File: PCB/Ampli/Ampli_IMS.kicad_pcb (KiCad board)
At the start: 2 copper layers, 67 x 32 mm, 22 parts, among them J1 5227161-3, J2 5227161-3, J3 Conn_01x03_Male, SW1 SS22D0205G2, U1 LT1464CS8, U2 LMP7721

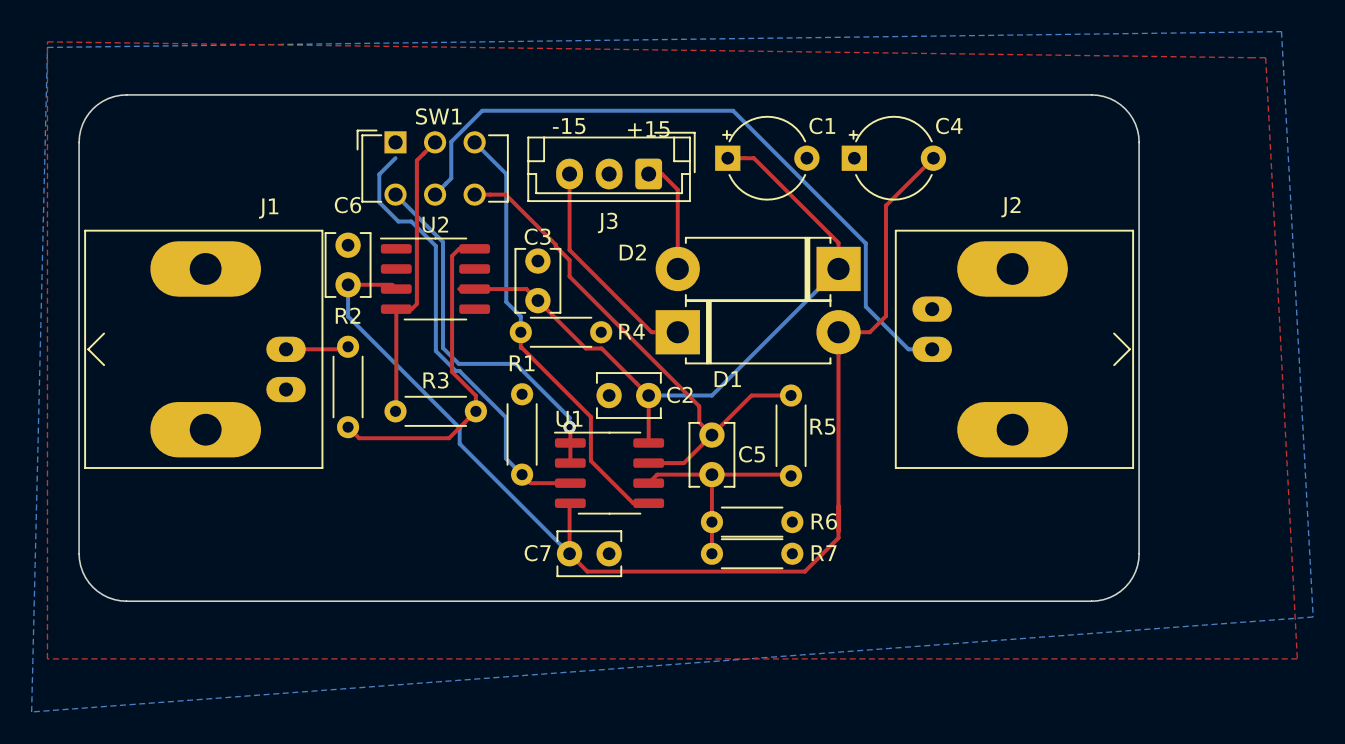
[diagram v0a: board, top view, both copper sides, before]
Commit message: Delete tracks
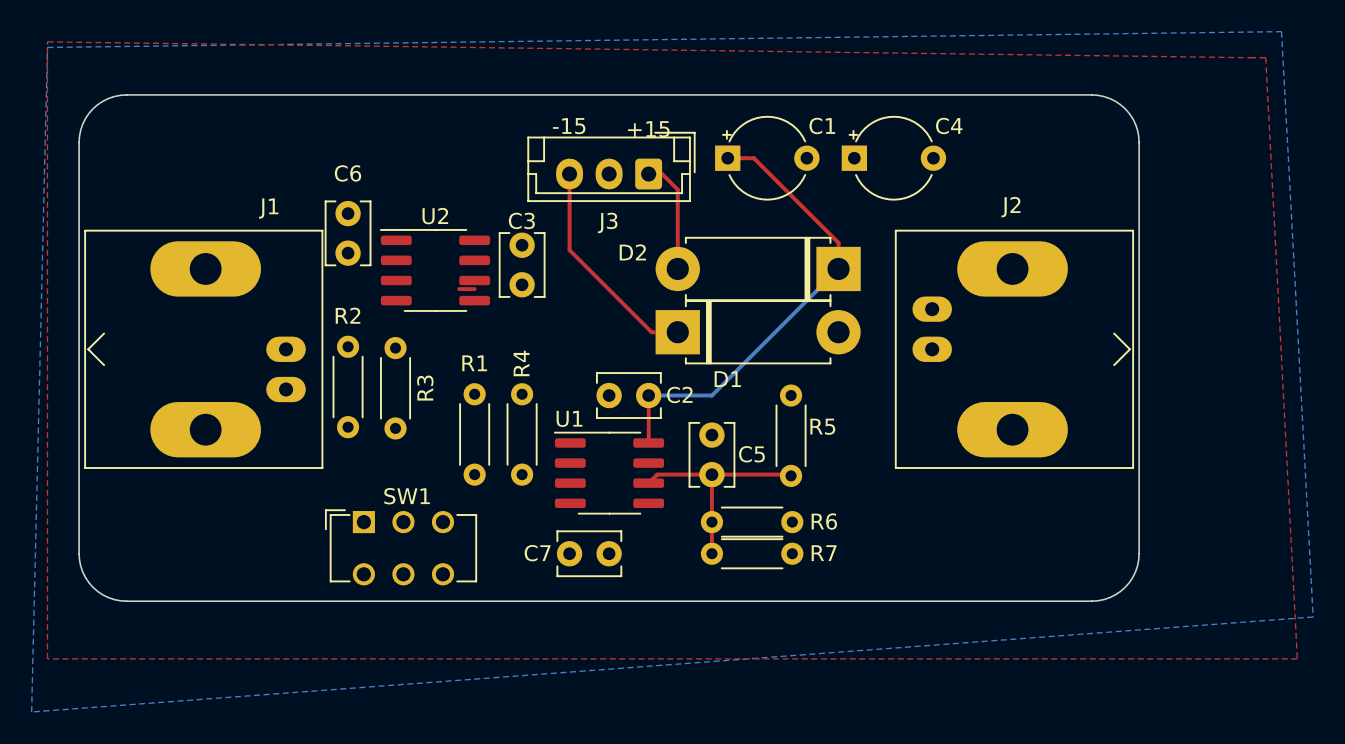
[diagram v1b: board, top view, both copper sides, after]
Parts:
- moved SW1 24.1 mm to (36.0, 45.0)
- moved R4 9.00 mm to (46.0, 42.0), turned to 90 degrees
- moved R3 4.00 mm to (38.0, 34.0), turned to 270 degrees
- moved R1 3.00 mm to (43.0, 42.0)
- moved C6 2.00 mm to (35.0, 28.0)
- moved C3 1.41 mm to (46.0, 30.0)
- moved U2 0.54 mm to (40.5, 29.1)
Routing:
- net /-15V: track 76.8 -> 0.00 mm
- net Net-(J2-Pad1): track 43.6 -> 0.00 mm
- net Net-(C5-Pad1): track 33.3 -> 0.00 mm
- net Net-(R1-Pad1): track 28.1 -> 0.00 mm
- net Net-(R4-Pad1): track 28.0 -> 0.00 mm
- net Net-(SW1-Pad4): track 23.7 -> 0.00 mm, vias 1 -> 0
- net Net-(R2-Pad1): track 21.1 -> 0.00 mm
- net Net-(R3-Pad1): track 18.7 -> 0.00 mm
- net /+15V: track 43.9 -> 30.2 mm
- net Net-(J1-Pad1): track 3.99 -> 0.00 mm

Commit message: Moved parts
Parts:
- moved C3 15.7 mm to (32.0, 23.0)
- moved R2 10.0 mm to (35.0, 29.0), turned to 270 degrees
- moved C6 9.85 mm to (44.0, 24.0)
- moved R3 6.40 mm to (42.0, 29.0), turned to 180 degrees
- moved U2 4.81 mm to (38.0, 25.0), turned to 180 degrees
- moved R1 2.83 mm to (41.0, 40.0)
- moved R4 2.83 mm to (44.0, 40.0)
- moved SW1 1.30 mm to (36.0, 43.7)
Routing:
- net /+15V: track 30.2 -> 10.9 mm
- net Net-(C5-Pad2): track 14.3 -> 10.0 mm

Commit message: tracks realised
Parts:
- removed the U2 at (38.0, 25.0)
- added U1: ADA4625-1, Package_SO:SO-8_3.9x4.9mm_P1.27mm, F.Cu at (37.4, 22.0)
- U2: renamed from U1; footprint Package_SO:SOIC-8_3.9x4.9mm_P1.27mm -> Package_SO:SO-8_3.9x4.9mm_P1.27mm
- moved R5 7.07 mm to (58.0, 42.0)
- moved R7 6.08 mm to (52.0, 48.0), turned to 180 degrees
- moved R6 6.00 mm to (52.0, 45.0), turned to 180 degrees
- moved C5 5.41 mm to (55.0, 44.0)
- moved C7 5.10 mm to (50.0, 42.0), turned to 180 degrees
- moved R4 5.00 mm to (44.0, 45.0)
- moved R3 4.47 mm to (38.0, 27.0), turned to 270 degrees
- moved U2 4.46 mm to (51.0, 37.5)
- moved C6 4.12 mm to (43.0, 20.0), turned to 270 degrees
- moved C2 3.16 mm to (57.0, 36.0), turned to 270 degrees
- moved D1 2.00 mm to (66.0, 27.0)
- moved D2 2.00 mm to (55.8, 31.0)
- moved C3 1.00 mm to (32.0, 22.0)
- moved SW1 1.00 mm to (35.0, 43.7)
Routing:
- net /-15V: track 0.00 -> 58.6 mm
- net /+15V: track 10.9 -> 60.3 mm
- net Net-(J2-Pad1): track 0.00 -> 42.4 mm
- net Net-(C5-Pad1): track 0.00 -> 29.1 mm
- net Net-(R3-Pad1): track 0.00 -> 24.9 mm
- net Net-(SW1-Pad4): track 0.00 -> 23.2 mm
- net Net-(C5-Pad2): track 10.0 -> 33.1 mm
- net Net-(R1-Pad1): track 0.00 -> 18.0 mm
- net Net-(R2-Pad1): track 0.00 -> 17.4 mm
- net Net-(R4-Pad1): track 0.00 -> 16.9 mm
- net Net-(J1-Pad1): track 0.23 -> 4.15 mm
- net GND: track 0.00 -> 3.06 mm
- net Net-(D1-Pad2): track 7.26 -> 5.26 mm
- net Net-(D2-Pad1): track 13.8 -> 11.9 mm
- removed copper zone on F.Cu, net GND

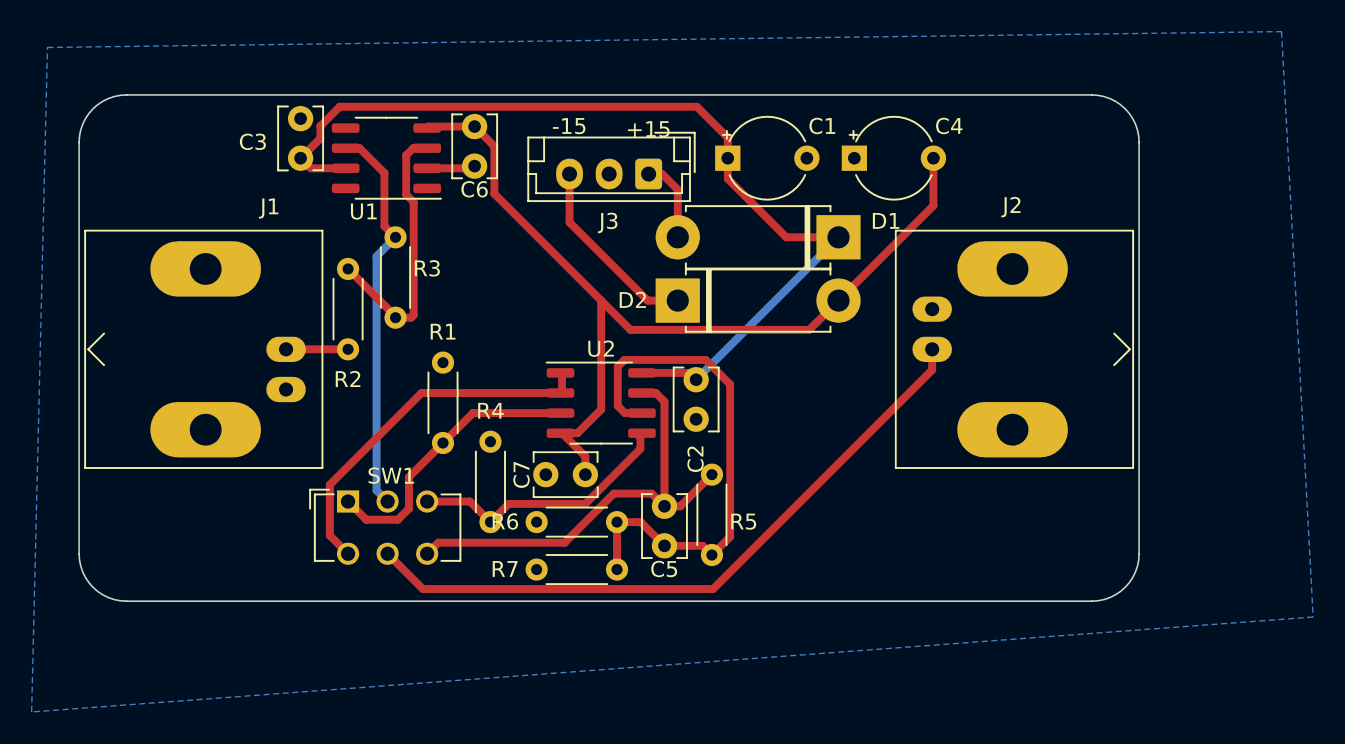
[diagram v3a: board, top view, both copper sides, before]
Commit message: Dimensions of pcb
Power parts brought together, and length of pcb smaller
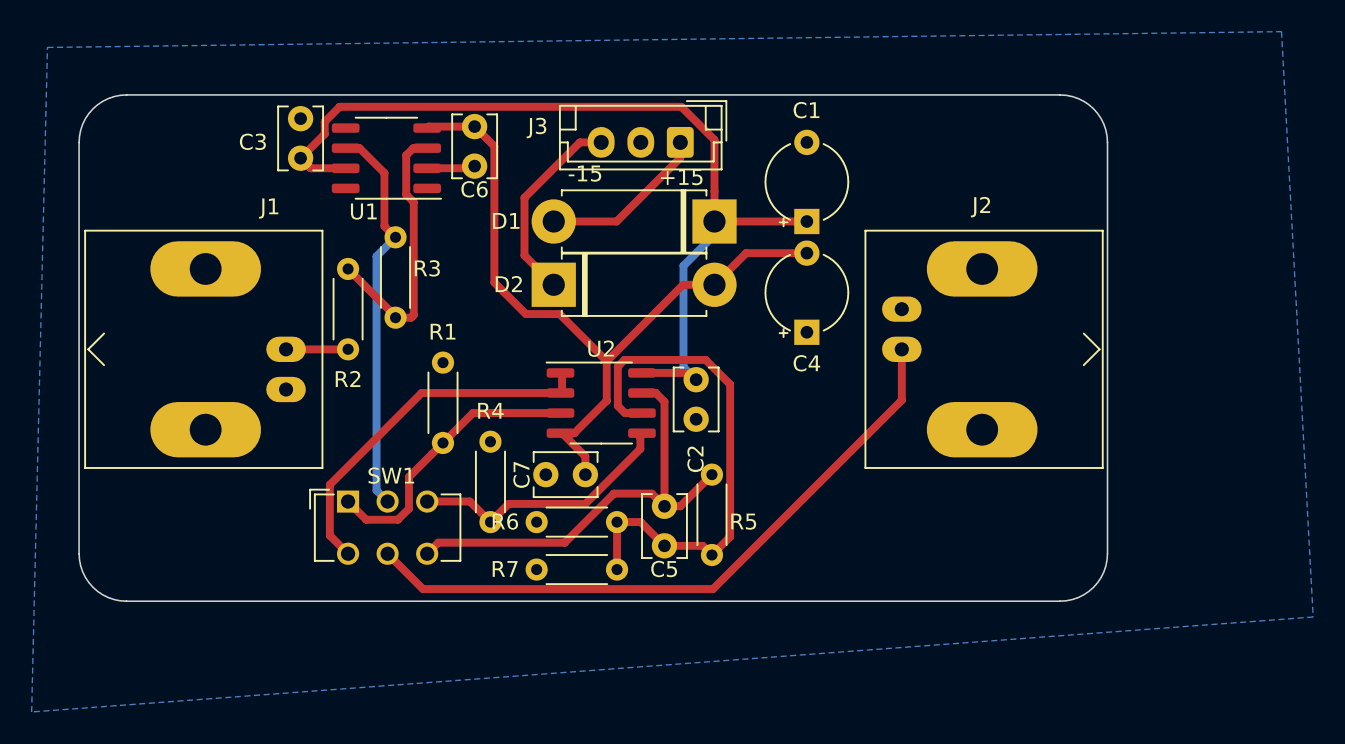
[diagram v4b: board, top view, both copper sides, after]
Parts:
- moved C4 11.4 mm to (64.0, 33.0), turned to 90 degrees
- moved D1 7.90 mm to (58.2, 26.0)
- moved D2 7.90 mm to (48.0, 30.0)
- moved C1 6.40 mm to (64.0, 26.0), turned to 90 degrees
- moved J3 2.83 mm to (56.0, 21.0)
- moved J2 1.92 mm to (70.0, 34.1)
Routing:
- net /-15V: track 58.6 -> 47.6 mm
- net Net-(D1-Pad2): track 5.26 -> 10.6 mm
- net /+15V: track 60.3 -> 57.8 mm
- net Net-(J2-Pad1): track 42.4 -> 41.6 mm
- net Net-(D2-Pad1): track 11.9 -> 12.6 mm
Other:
- board size 67 x 32 mm -> 65 x 32 mm
